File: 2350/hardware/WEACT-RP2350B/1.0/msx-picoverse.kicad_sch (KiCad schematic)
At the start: 13 parts, among them J1 Micro_SD_Card, U1 WEACT-RP2350B

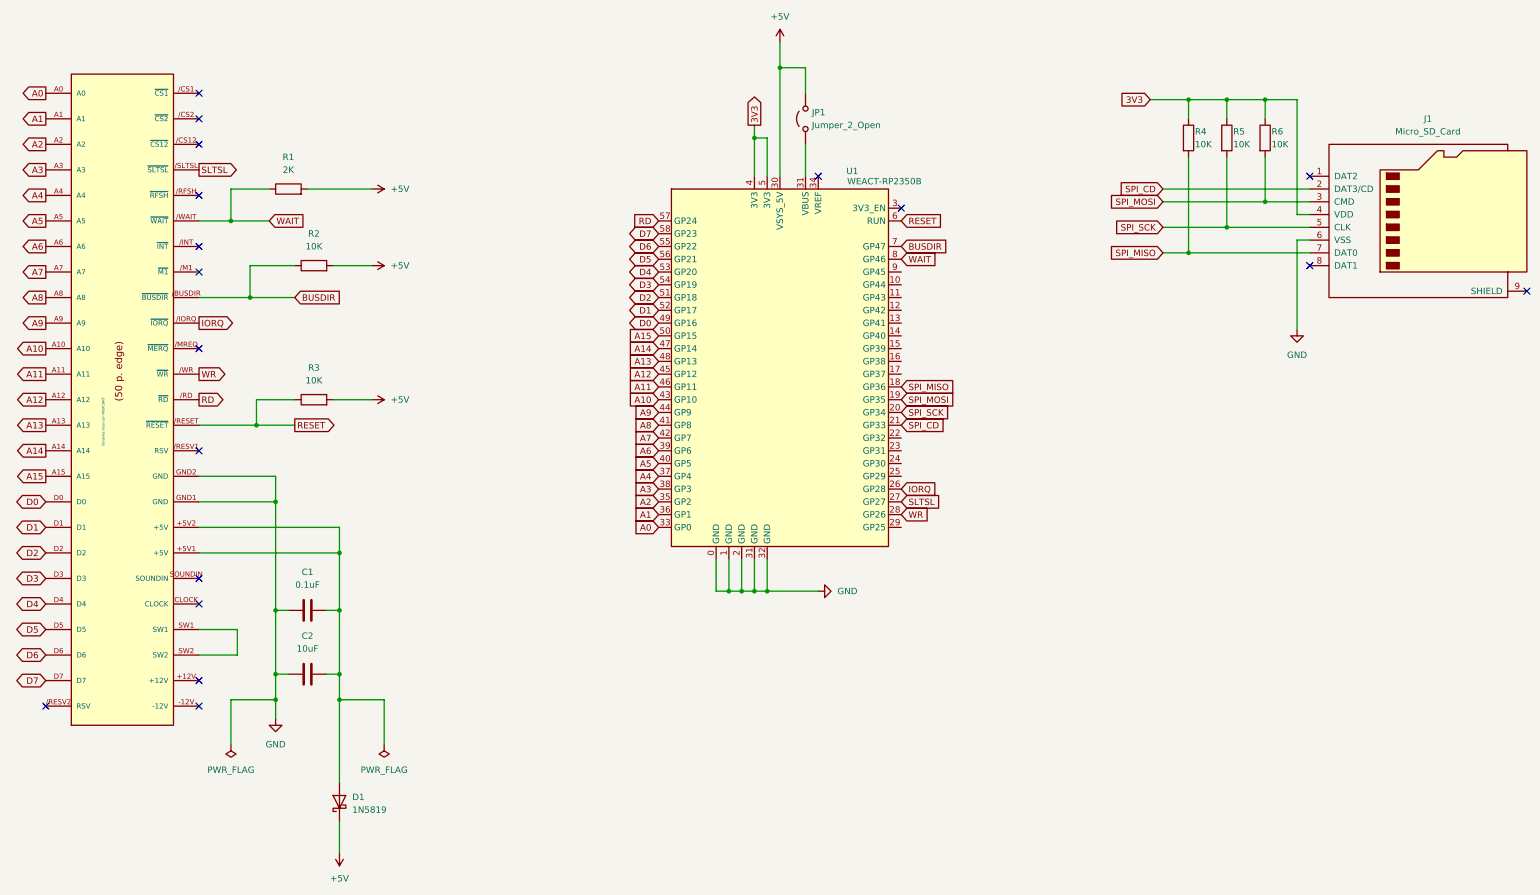
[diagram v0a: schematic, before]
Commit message: Sound added to the schematic
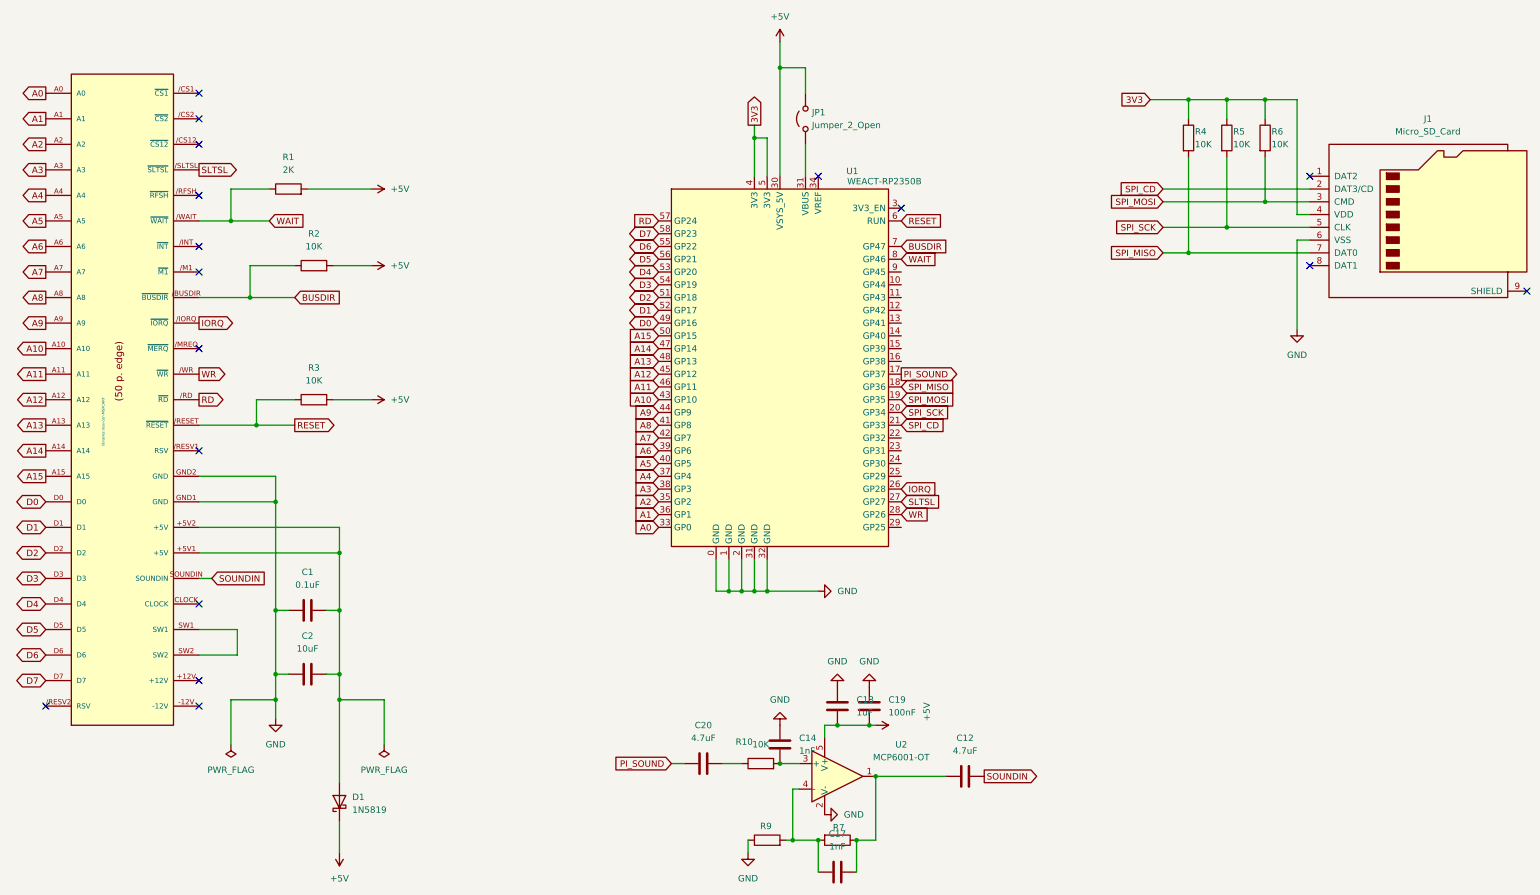
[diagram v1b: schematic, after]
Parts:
- added C12, C20: 4.7uF, Capacitor_SMD:C_0603_1608Metric_Pad1.08x0.95mm_HandSolder, symbol Device:C
- added C14, C17: 1nF, Capacitor_SMD:C_0603_1608Metric_Pad1.08x0.95mm_HandSolder, symbol Device:C
- added C18: 1uF, Capacitor_SMD:C_0603_1608Metric_Pad1.08x0.95mm_HandSolder, symbol Device:C
- added C19: 100nF, Capacitor_SMD:C_0603_1608Metric_Pad1.08x0.95mm_HandSolder, symbol Device:C
- added R10, R7, R9: 10K, Resistor_SMD:R_0603_1608Metric_Pad0.98x0.95mm_HandSolder, symbol Device:R
- added U2: MCP6001-OT, Package_TO_SOT_SMD:SOT-23-5, symbol Amplifier_Operational:MCP6001-OT
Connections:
- net +5V: now also C18.2, C19.2, U2.5 (V+)
- net GND: now also C14.2, C18.1, C19.1, R9.1, U2.2 (V-)
- net PI_SOUND: now reaches U1.17 (GP37)
- net PI_SOUND: now also C20.1
- net SOUNDIN: now reaches EDG1.SOUNDIN
- net SOUNDIN: now also C12.2
- new net: C20.2, R10.1
- new net: C14.1, R10.2, U2.3 (+)
- new net: C12.1, C17.2, R7.1, U2.1
- new net: C17.1, R7.2, R9.2, U2.4 (-)
- no-connect marks 18 -> 17

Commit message: My first cartridge
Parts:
- removed J1: Micro_SD_Card, symbol Connector:Micro_SD_Card
- removed U1: WEACT-RP2350B, symbol WeAct:RP2350B
- added J2: Micro_SD_Card, Connector_Card:microSD_HC_Molex_47219-2001, symbol Connector:Micro_SD_Card
- added U3: ~, WEACT_RP2350b:WeAct_RP2350B_headers, symbol WeAct:RP2350B
- R4, R5, R6: footprint (none) -> Resistor_SMD:R_0603_1608Metric_Pad0.98x0.95mm_HandSolder
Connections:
- net +5V: now also U3.30 (VSYS_5V)
- net 3V3: now also J2.4 (VDD), U3.4 (3V3), U3.5 (3V3)
- net A0: now also U3.34 (GP0)
- net A1: now also U3.37 (GP1)
- net A10: now also U3.44 (GP10)
- net A11: now also U3.47 (GP11)
- net A12: now also U3.46 (GP12)
- net A13: now also U3.49 (GP13)
- net A14: now also U3.48 (GP14)
- net A15: now also U3.51 (GP15)
- net A2: now also U3.36 (GP2)
- net A3: now also U3.39 (GP3)
- net A4: now also U3.38 (GP4)
- net A5: now also U3.41 (GP5)
- net A6: now also U3.40 (GP6)
- net A7: now also U3.43 (GP7)
- net A8: now also U3.42 (GP8)
- net A9: now also U3.45 (GP9)
- net BUSDIR: now also U3.7 (GP47)
- net D0: now also U3.50 (GP16)
- net D1: now also U3.53 (GP17)
- net D2: now also U3.52 (GP18)
- net D3: now also U3.55 (GP19)
- net D4: now also U3.54 (GP20)
- net D5: now also U3.57 (GP21)
- net D6: now also U3.56 (GP22)
- net D7: now also U3.59 (GP23)
- net GND: now also J2.6 (VSS), U3.0 (GND), U3.1 (GND), U3.2 (GND), U3.32 (GND), U3.33 (GND)
- net IORQ: now also U3.26 (GP28)
- net PI_SOUND: now also U3.17 (GP37)
- net RD: now also U3.58 (GP24)
- net RESET: now also U3.6 (RUN)
- net SLTSL: now also U3.27 (GP27)
- net SPI_CD: now also J2.2 (DAT3/CD), U3.21 (GP33)
- net SPI_MISO: now also J2.7 (DAT0), U3.18 (GP36)
- net SPI_MOSI: now also J2.3 (CMD), U3.19 (GP35)
- net SPI_SCK: now also J2.5 (CLK), U3.20 (GP34)
- net WAIT: now also U3.8 (GP46)
- net WR: now also U3.28 (GP26)
- net at JP1.1 (A): now also U3.31 (VBUS)
- no-connect marks 17 -> 29
